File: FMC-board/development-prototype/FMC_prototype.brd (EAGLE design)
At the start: 103.8 x 69.8 mm, 65 parts, among them J1 DC_POWER_JACK-PJ-102AH, J2 DC_POWER_JACK-PJ-102AH

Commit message: routed nonisolated A SPI connector
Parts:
- moved R1 7.12 mm to (51.6, 59.1), turned to 180 degrees
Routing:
- net MISO1+: track 17.4 -> 98.6 mm, vias 1 -> 6
- net MISO2+: track 0.00 -> 79.6 mm, vias 0 -> 4
- net SCLK-: track 0.00 -> 79.5 mm, vias 0 -> 1
- net CS-: track 0.00 -> 79.0 mm, vias 0 -> 1
- net MISO1-: track 0.00 -> 75.9 mm, vias 0 -> 4
- net CS+: track 0.00 -> 75.8 mm, vias 0 -> 3
- net SCLK+: track 0.00 -> 74.3 mm, vias 0 -> 3
- net MISO2-: track 0.00 -> 72.3 mm, vias 0 -> 3
- net MOSI+: track 34.2 -> 101.5 mm, vias 0 -> 2
- net MOSI-: track 0.00 -> 66.5 mm, vias 0 -> 1
- net GND: track 77.4 -> 97.8 mm, vias 5 -> 8
- net N$35: track 13.7 -> 7.49 mm
- net VDD36: track 79.6 -> 85.7 mm
- net VDD33: track 137.5 -> 135.4 mm
- net GND_ISOLATED: track 76.6 -> 77.2 mm

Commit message: connected B SPI
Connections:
- removed net N$17: B.B5
- removed net N$18: B.T5
- removed net N$19: B.B4
- removed net N$20: B.T4
- removed net N$21: B.B3
- removed net N$22: B.T3
- removed net N$23: B.B2
- removed net N$24: B.T2
- removed net N$25: B.B1
- removed net N$26: B.T1
- new net B_CS+: B.B1, U$4.P$37
- new net B_CS-: B.T1, U$4.P$38
- new net B_MISO1+: B.B4, U$4.P$28
- new net B_MISO1-: B.T4, U$4.P$29
- new net B_MISO2+: B.B5, U$4.P$25
- new net B_MISO2-: B.T5, U$4.P$26
- new net B_MOSI+: B.B3, U$4.P$31
- new net B_MOSI-: B.T3, U$4.P$32
- new net B_SCLK+: B.B2, U$4.P$34
- new net B_SCLK-: B.T2, U$4.P$35
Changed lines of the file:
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@@
 <wire x1="40.64" y1="64.77" x2="31.6865" y2="64.77" width="0" layer="19" extent="1-16"/>
-</signal>
-<signal name="N$17">
-<contactref element="B" pad="B5"/>
-</signal>
-<signal name="N$18">
-<contactref element="B" pad="T5"/>
-</signal>
-<signal name="N$19">
-<contactref element="B" pad="B4"/>
-</signal>
-<signal name="N$20">
-<contactref element="B" pad="T4"/>
-</signal>
-<signal name="N$21">
-<contactref element="B" pad="B3"/>
-</signal>
-<signal name="N$22">
-<contactref element="B" pad="T3"/>
-</signal>
-<signal name="N$23">
-<contactref element="B" pad="B2"/>
-</signal>
-<signal name="N$24">
-<contactref element="B" pad="T2"/>
-</signal>
-<signal name="N$25">
-<contactref element="B" pad="B1"/>
-</signal>
-<signal name="N$26">
-<contactref element="B" pad="T1"/>
 </signal>
 <signal name="N$14">
@@
 <wire x1="54.356" y1="18.796" x2="54.356" y2="18.114" width="0.3048" layer="1"/>
 </signal>
+<signal name="B_MISO2+">
+<contactref element="U$4" pad="P$25"/>
+<contactref element="B" pad="B5"/>
+<wire x1="21.59" y1="40.64" x2="32.3215" y2="64.77" width="0" layer="19" extent="1-16"/>
+</signal>
+<signal name="B_MISO2-">
+<contactref element="U$4" pad="P$26"/>
+<contactref element="B" pad="T5"/>
+<wire x1="21.59" y1="41.91" x2="32.3215" y2="63.627" width="0" layer="19" extent="1-16"/>
+</signal>
+<signal name="B_MISO1+">
+<contactref element="U$4" pad="P$28"/>
+<contactref element="B" pad="B4"/>
+<wire x1="21.59" y1="44.45" x2="32.9565" y2="64.77" width="0" layer="19" extent="1-16"/>
+</signal>
+<signal name="B_MISO1-">
+<contactref element="U$4" pad="P$29"/>
+<contactref element="B" pad="T4"/>
+<wire x1="21.59" y1="45.72" x2="32.9565" y2="63.627" width="0" layer="19" extent="1-16"/>
+</signal>
+<signal name="B_MOSI+">
+<contactref element="U$4" pad="P$31"/>
+<contactref element="B" pad="B3"/>
+<wire x1="21.59" y1="48.26" x2="33.5915" y2="64.77" width="0" layer="19" extent="1-16"/>
+</signal>
+<signal name="B_MOSI-">
+<contactref element="U$4" pad="P$32"/>
+<contactref element="B" pad="T3"/>
+<wire x1="21.59" y1="49.53" x2="33.5915" y2="63.627" width="0" layer="19" extent="1-16"/>
+</signal>
+<signal name="B_SCLK+">
+<contactref element="U$4" pad="P$34"/>
+<contactref element="B" pad="B2"/>
+<wire x1="21.59" y1="52.07" x2="34.2265" y2="64.77" width="0" layer="19" extent="1-16"/>
+</signal>
+<signal name="B_SCLK-">
+<contactref element="U$4" pad="P$35"/>
+<contactref element="B" pad="T2"/>
+<wire x1="21.59" y1="53.34" x2="34.2265" y2="63.627" width="0" layer="19" extent="1-16"/>
+</signal>
+<signal name="B_CS+">
+<contactref element="U$4" pad="P$37"/>
+<contactref element="B" pad="B1"/>
+<wire x1="21.59" y1="55.88" x2="34.8615" y2="64.77" width="0" layer="19" extent="1-16"/>
+</signal>
+<signal name="B_CS-">
+<contactref element="U$4" pad="P$38"/>
+<contactref element="B" pad="T1"/>
+<wire x1="21.59" y1="57.15" x2="34.8615" y2="63.627" width="0" layer="19" extent="1-16"/>
+</signal>
 </signals>

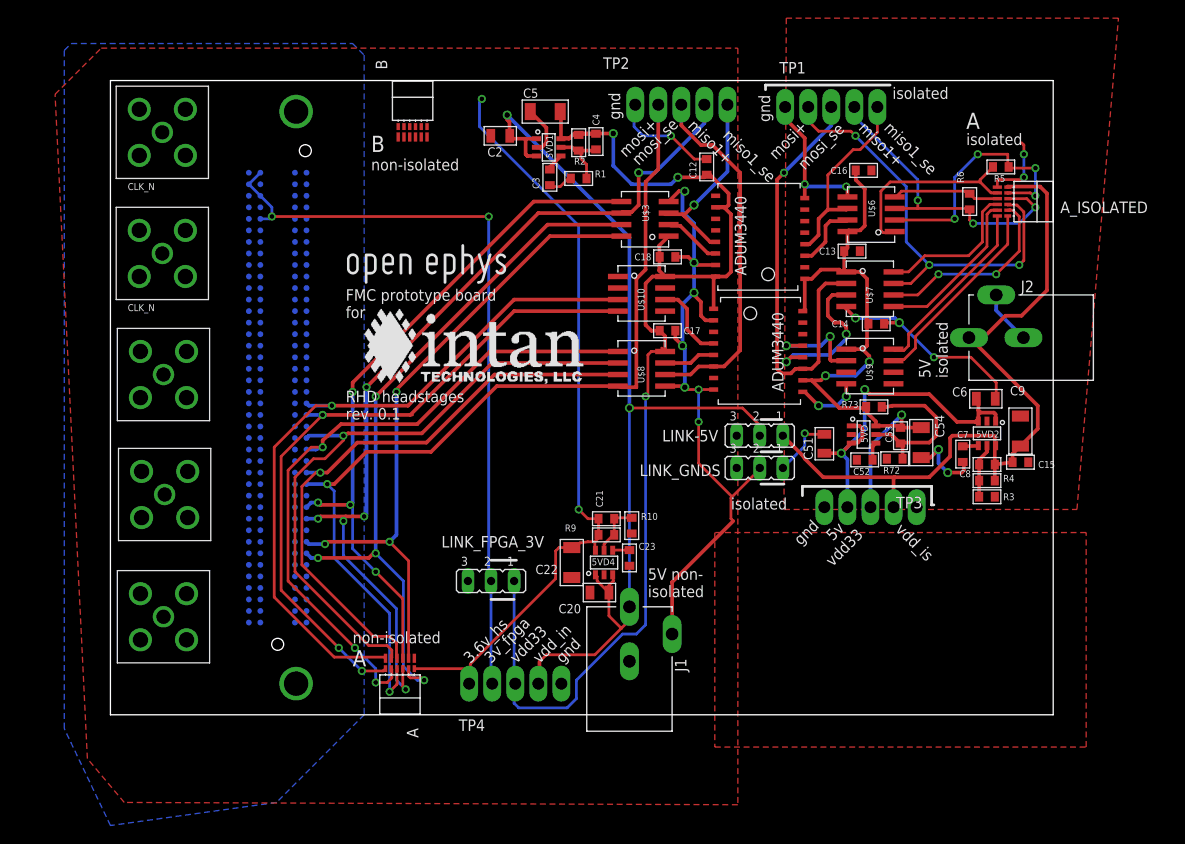
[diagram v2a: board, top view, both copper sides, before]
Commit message: routed B SPI connector
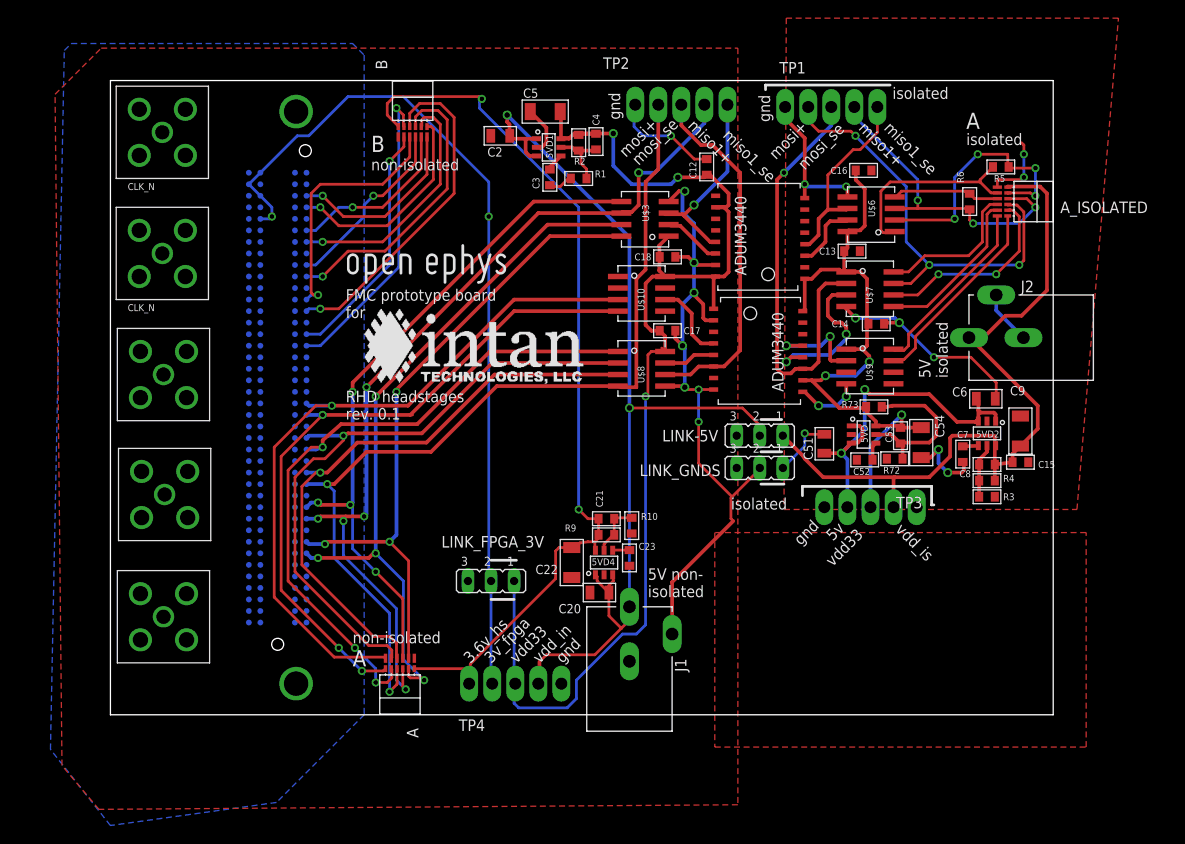
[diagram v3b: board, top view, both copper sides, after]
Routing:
- net B_MISO1+: track 0.00 -> 37.4 mm, vias 0 -> 1
- net B_MISO2+: track 0.00 -> 33.7 mm, vias 0 -> 1
- net B_MOSI+: track 0.00 -> 32.4 mm, vias 0 -> 1
- net B_MISO1-: track 0.00 -> 28.0 mm, vias 0 -> 1
- net B_SCLK+: track 0.00 -> 27.2 mm, vias 0 -> 1
- net B_MISO2-: track 0.00 -> 27.1 mm, vias 0 -> 1
- net B_CS+: track 0.00 -> 23.3 mm, vias 0 -> 1
- net B_CS-: track 0.00 -> 20.3 mm, vias 0 -> 1
- net B_MOSI-: track 0.00 -> 20.3 mm, vias 0 -> 1
- net B_SCLK-: track 0.00 -> 18.9 mm, vias 0 -> 1
- net VDD36: track 85.7 -> 99.5 mm
- net 3V_FPGA: track 83.8 -> 96.2 mm

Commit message: small cleanups
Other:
- outline, holes or cut-outs redrawn
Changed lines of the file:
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@@
 <setting verticaltext="up"/>
 </settings>
-<grid distance="0.01" unitdist="inch" unit="inch" style="dots" multiple="1" display="yes" altdistance="0.0125" altunitdist="inch" altunit="inch"/>
+<grid distance="0.01" unitdist="inch" unit="inch" style="lines" multiple="1" display="yes" altdistance="0.0125" altunitdist="inch" altunit="inch"/>
 <layers>
 <layer number="1" name="Top" color="42" fill="1" visible="yes" active="yes"/>
@@
 <board>
 <plain>
-<wire x1="0" y1="0" x2="103.81" y2="0" width="0" layer="20"/>
-<wire x1="103.81" y1="0" x2="103.81" y2="69.84" width="0" layer="20"/>
-<wire x1="103.81" y1="69.84" x2="0" y2="69.84" width="0" layer="20"/>
+<wire x1="0" y1="0" x2="98.806" y2="0" width="0" layer="20"/>
+<wire x1="98.806" y1="0" x2="98.984" y2="0.178" width="0" layer="20"/>
+<wire x1="98.984" y1="0.178" x2="103.81" y2="5.08" width="0" layer="20"/>
+<wire x1="103.81" y1="5.08" x2="103.81" y2="64.76" width="0" layer="20"/>
+<wire x1="103.81" y1="64.76" x2="98.816" y2="69.84" width="0" layer="20"/>
+<wire x1="98.816" y1="69.84" x2="98.806" y2="69.85" width="0" layer="20"/>
+<wire x1="98.806" y1="69.85" x2="0" y2="69.84" width="0" layer="20"/>
 <wire x1="0" y1="69.84" x2="0" y2="0" width="0" layer="20"/>
 <text x="1.905" y="57.785" size="0.762" layer="21">CLK_N</text>
@@
 <wire x1="57.658" y1="64.77" x2="57.658" y2="67.056" width="0.3048" layer="16"/>
 <wire x1="57.658" y1="67.056" x2="57.785" y2="67.183" width="0.3048" layer="16"/>
+<wire x1="21.59" y1="50.8" x2="21.59" y2="54.61" width="0" layer="19" extent="16-16"/>
+<wire x1="21.59" y1="46.99" x2="21.59" y2="50.8" width="0" layer="19" extent="16-16"/>
+<wire x1="21.59" y1="39.37" x2="21.59" y2="43.18" width="0" layer="19" extent="16-16"/>
 <wire x1="21.59" y1="27.94" x2="21.59" y2="31.75" width="0" layer="19" extent="16-16"/>
 <wire x1="21.59" y1="24.13" x2="21.59" y2="27.94" width="0" layer="19" extent="16-16"/>
+<wire x1="15.24" y1="54.61" x2="21.59" y2="54.61" width="0" layer="19" extent="16-16"/>
 </signal>
 <signal name="MISO2+">
@@
 <contactref element="A_ISOLATED" pad="T1"/>
 <wire x1="97.663" y1="54.9275" x2="97.663" y2="51.689" width="0.3048" layer="1"/>
-<wire x1="97.663" y1="51.689" x2="87.884" y2="41.91" width="0.3048" layer="1"/>
-<wire x1="87.884" y1="41.91" x2="87.884" y2="40.64" width="0.3048" layer="1"/>
-<wire x1="87.884" y1="40.64" x2="87.376" y2="40.132" width="0.3048" layer="1"/>
+<wire x1="97.663" y1="51.689" x2="87.63" y2="41.656" width="0.3048" layer="1"/>
+<wire x1="87.63" y1="41.656" x2="87.63" y2="40.386" width="0.3048" layer="1"/>
+<wire x1="87.63" y1="40.386" x2="87.376" y2="40.132" width="0.3048" layer="1"/>
 <wire x1="87.376" y1="40.132" x2="86.353" y2="40.132" width="0.3048" layer="1"/>
 <wire x1="86.353" y1="40.132" x2="86.226" y2="40.259" width="0.3048" layer="1"/>
@@
 <wire x1="81.026" y1="47.498" x2="78.74" y2="47.498" width="0.4064" layer="1"/>
 <wire x1="78.74" y1="47.498" x2="77.978" y2="46.736" width="0.4064" layer="1"/>
-<wire x1="77.978" y1="46.736" x2="77.978" y2="38.862" width="0.4064" layer="1"/>
-<wire x1="77.978" y1="38.862" x2="77.216" y2="38.1" width="0.4064" layer="1"/>
-<wire x1="77.216" y1="38.1" x2="76.235" y2="38.1" width="0.4064" layer="1"/>
+<wire x1="77.978" y1="46.736" x2="77.978" y2="39.116" width="0.4064" layer="1"/>
+<wire x1="77.978" y1="39.116" x2="76.962" y2="38.1" width="0.4064" layer="1"/>
+<wire x1="76.962" y1="38.1" x2="76.235" y2="38.1" width="0.4064" layer="1"/>
 <wire x1="79.375" y1="66.929" x2="79.375" y2="64.897" width="0.4064" layer="16"/>
 <wire x1="79.375" y1="64.897" x2="74.168" y2="59.69" width="0.4064" layer="16"/>
@@
 <contactref element="U$9" pad="P7"/>
 <wire x1="98.806" y1="54.9275" x2="98.806" y2="51.816" width="0.3048" layer="1"/>
-<wire x1="98.806" y1="51.816" x2="88.646" y2="41.656" width="0.3048" layer="1"/>
-<wire x1="88.646" y1="41.656" x2="88.646" y2="40.386" width="0.3048" layer="1"/>
-<wire x1="88.646" y1="40.386" x2="87.376" y2="39.116" width="0.3048" layer="1"/>
+<wire x1="98.806" y1="51.816" x2="88.392" y2="41.402" width="0.3048" layer="1"/>
+<wire x1="88.392" y1="41.402" x2="88.392" y2="40.132" width="0.3048" layer="1"/>
+<wire x1="88.392" y1="40.132" x2="87.376" y2="39.116" width="0.3048" layer="1"/>
 <wire x1="87.376" y1="39.116" x2="86.353" y2="39.116" width="0.3048" layer="1"/>
 <wire x1="86.353" y1="39.116" x2="86.226" y2="38.989" width="0.3048" layer="1"/>

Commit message: more small cleanups
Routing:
- net MOSI-: track 66.5 -> 65.6 mm
- net CS-: track 79.0 -> 78.3 mm
- net MOSI+: track 101.5 -> 102.0 mm
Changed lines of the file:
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@@
 <setting verticaltext="up"/>
 </settings>
-<grid distance="0.01" unitdist="inch" unit="inch" style="lines" multiple="1" display="yes" altdistance="0.0125" altunitdist="inch" altunit="inch"/>
+<grid distance="0.02" unitdist="inch" unit="inch" style="lines" multiple="1" display="yes" altdistance="0.0125" altunitdist="inch" altunit="inch"/>
 <layers>
 <layer number="1" name="Top" color="42" fill="1" visible="yes" active="yes"/>
-<layer number="16" name="Bottom" color="1" fill="1" visible="yes" active="yes"/>
+<layer number="16" name="Bottom" color="1" fill="1" visible="no" active="yes"/>
 <layer number="17" name="Pads" color="2" fill="1" visible="yes" active="yes"/>
 <layer number="18" name="Vias" color="2" fill="1" visible="yes" active="yes"/>
@@
 <wire x1="25.654" y1="30.226" x2="23.622" y2="28.194" width="0.3048" layer="1"/>
 <wire x1="23.622" y1="28.194" x2="22.352" y2="28.194" width="0.3048" layer="1"/>
-<wire x1="22.352" y1="28.194" x2="20.32" y2="26.162" width="0.3048" layer="1"/>
-<wire x1="20.32" y1="26.162" x2="20.32" y2="15.748" width="0.3048" layer="1"/>
-<wire x1="20.32" y1="15.748" x2="28.448" y2="7.62" width="0.3048" layer="1"/>
+<wire x1="22.352" y1="28.194" x2="20.828" y2="26.67" width="0.3048" layer="1"/>
+<wire x1="20.828" y1="26.67" x2="20.828" y2="15.24" width="0.3048" layer="1"/>
+<wire x1="20.828" y1="15.24" x2="28.448" y2="7.62" width="0.3048" layer="1"/>
 <wire x1="28.448" y1="7.62" x2="30.48" y2="7.62" width="0.3048" layer="1"/>
 <wire x1="30.48" y1="7.62" x2="30.988" y2="7.112" width="0.3048" layer="1"/>
@@
 <wire x1="22.606" y1="29.21" x2="21.59" y2="29.21" width="0.4064" layer="16"/>
 <wire x1="23.368" y1="29.464" x2="22.098" y2="29.464" width="0.3048" layer="1"/>
-<wire x1="22.098" y1="29.464" x2="19.558" y2="26.924" width="0.3048" layer="1"/>
-<wire x1="19.558" y1="26.924" x2="19.558" y2="14.732" width="0.3048" layer="1"/>
-<wire x1="19.558" y1="14.732" x2="26.924" y2="7.366" width="0.3048" layer="1"/>
+<wire x1="22.098" y1="29.464" x2="20.066" y2="27.432" width="0.3048" layer="1"/>
+<wire x1="20.066" y1="27.432" x2="20.066" y2="14.224" width="0.3048" layer="1"/>
+<wire x1="20.066" y1="14.224" x2="26.924" y2="7.366" width="0.3048" layer="1"/>
 <via x="26.924" y="7.366" extent="1-16" drill="0.5"/>
 <wire x1="26.924" y1="7.366" x2="29.21" y2="5.08" width="0.3048" layer="16"/>
@@
 <wire x1="55.88" y1="37.465" x2="42.291" y2="37.465" width="0.4064" layer="1"/>
 <wire x1="42.291" y1="37.465" x2="34.798" y2="29.972" width="0.4064" layer="1"/>
-<wire x1="34.798" y1="29.972" x2="27.178" y2="29.972" width="0.4064" layer="1"/>
-<wire x1="27.178" y1="29.972" x2="23.876" y2="26.67" width="0.4064" layer="1"/>
-<wire x1="23.876" y1="26.67" x2="23.114" y2="26.67" width="0.4064" layer="1"/>
+<wire x1="34.798" y1="29.972" x2="26.67" y2="29.972" width="0.4064" layer="1"/>
+<wire x1="26.67" y1="29.972" x2="23.368" y2="26.67" width="0.4064" layer="1"/>
+<wire x1="23.368" y1="26.67" x2="23.114" y2="26.67" width="0.4064" layer="1"/>
 <via x="23.114" y="26.67" extent="1-16" drill="0.5"/>
 <wire x1="23.114" y1="26.67" x2="21.59" y2="26.67" width="0.4064" layer="16"/>
-<wire x1="23.876" y1="26.67" x2="22.606" y2="26.67" width="0.3048" layer="1"/>
-<wire x1="22.606" y1="26.67" x2="21.082" y2="25.146" width="0.3048" layer="1"/>
-<wire x1="21.082" y1="25.146" x2="21.082" y2="16.51" width="0.3048" layer="1"/>
-<wire x1="21.082" y1="16.51" x2="28.956" y2="8.636" width="0.3048" layer="1"/>
+<wire x1="23.368" y1="26.67" x2="22.606" y2="26.67" width="0.3048" layer="1"/>
+<wire x1="22.606" y1="26.67" x2="21.59" y2="25.654" width="0.3048" layer="1"/>
+<wire x1="21.59" y1="25.654" x2="21.59" y2="16.002" width="0.3048" layer="1"/>
+<wire x1="21.59" y1="16.002" x2="28.956" y2="8.636" width="0.3048" layer="1"/>
 <wire x1="28.956" y1="8.636" x2="30.734" y2="8.636" width="0.3048" layer="1"/>
 <wire x1="30.734" y1="8.636" x2="31.496" y2="7.874" width="0.3048" layer="1"/>
@@
 <wire x1="55.88" y1="36.195" x2="42.545" y2="36.195" width="0.4064" layer="1"/>
 <wire x1="42.545" y1="36.195" x2="35.306" y2="28.956" width="0.4064" layer="1"/>
-<wire x1="35.306" y1="28.956" x2="28.194" y2="28.956" width="0.4064" layer="1"/>
-<wire x1="28.194" y1="28.956" x2="24.638" y2="25.4" width="0.4064" layer="1"/>
-<wire x1="24.638" y1="25.4" x2="23.876" y2="25.4" width="0.4064" layer="1"/>
+<wire x1="35.306" y1="28.956" x2="27.178" y2="28.956" width="0.4064" layer="1"/>
+<wire x1="27.178" y1="28.956" x2="23.622" y2="25.4" width="0.4064" layer="1"/>
+<wire x1="23.622" y1="25.4" x2="23.876" y2="25.4" width="0.4064" layer="1"/>
 <via x="23.876" y="25.4" extent="1-16" drill="0.5"/>
 <wire x1="23.876" y1="25.4" x2="21.59" y2="25.4" width="0.4064" layer="16"/>
@@
 <wire x1="24.384" y1="34.036" x2="21.844" y2="34.036" width="0.4064" layer="16"/>
 <wire x1="21.844" y1="34.036" x2="21.59" y2="34.29" width="0.4064" layer="16"/>
-<wire x1="24.384" y1="34.036" x2="22.606" y2="34.036" width="0.3048" layer="1"/>
-<wire x1="22.606" y1="34.036" x2="18.034" y2="29.464" width="0.3048" layer="1"/>
-<wire x1="18.034" y1="29.464" x2="18.034" y2="12.954" width="0.3048" layer="1"/>
-<wire x1="18.034" y1="12.954" x2="24.638" y2="6.35" width="0.3048" layer="1"/>
+<wire x1="24.384" y1="34.036" x2="23.114" y2="34.036" width="0.3048" layer="1"/>
+<wire x1="23.114" y1="34.036" x2="18.542" y2="29.464" width="0.3048" layer="1"/>
+<wire x1="18.542" y1="29.464" x2="18.542" y2="12.446" width="0.3048" layer="1"/>
+<wire x1="18.542" y1="12.446" x2="24.638" y2="6.35" width="0.3048" layer="1"/>
 <wire x1="24.638" y1="6.35" x2="30.1625" y2="6.35" width="0.3048" layer="1"/>
 <wire x1="30.1625" y1="6.35" x2="30.2895" y2="6.223" width="0.3048" layer="1"/>
@@
 <wire x1="23.368" y1="33.02" x2="21.59" y2="33.02" width="0.4064" layer="16"/>
 <wire x1="33.02" y1="33.02" x2="33.274" y2="33.02" width="0.3048" layer="1"/>
-<wire x1="23.368" y1="33.02" x2="18.796" y2="28.448" width="0.3048" layer="1"/>
-<wire x1="18.796" y1="28.448" x2="18.796" y2="13.716" width="0.3048" layer="1"/>
-<wire x1="18.796" y1="13.716" x2="25.146" y2="7.366" width="0.3048" layer="1"/>
+<wire x1="23.368" y1="33.02" x2="19.304" y2="28.956" width="0.3048" layer="1"/>
+<wire x1="19.304" y1="28.956" x2="19.304" y2="13.208" width="0.3048" layer="1"/>
+<wire x1="19.304" y1="13.208" x2="25.146" y2="7.366" width="0.3048" layer="1"/>
 <via x="25.146" y="7.366" extent="1-16" drill="0.5"/>
 <wire x1="25.146" y1="7.366" x2="27.686" y2="4.826" width="0.3048" layer="16"/>
